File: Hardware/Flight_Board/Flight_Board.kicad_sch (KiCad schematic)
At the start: 5 parts, among them J1 Conn_01x04, J2 Conn_01x08

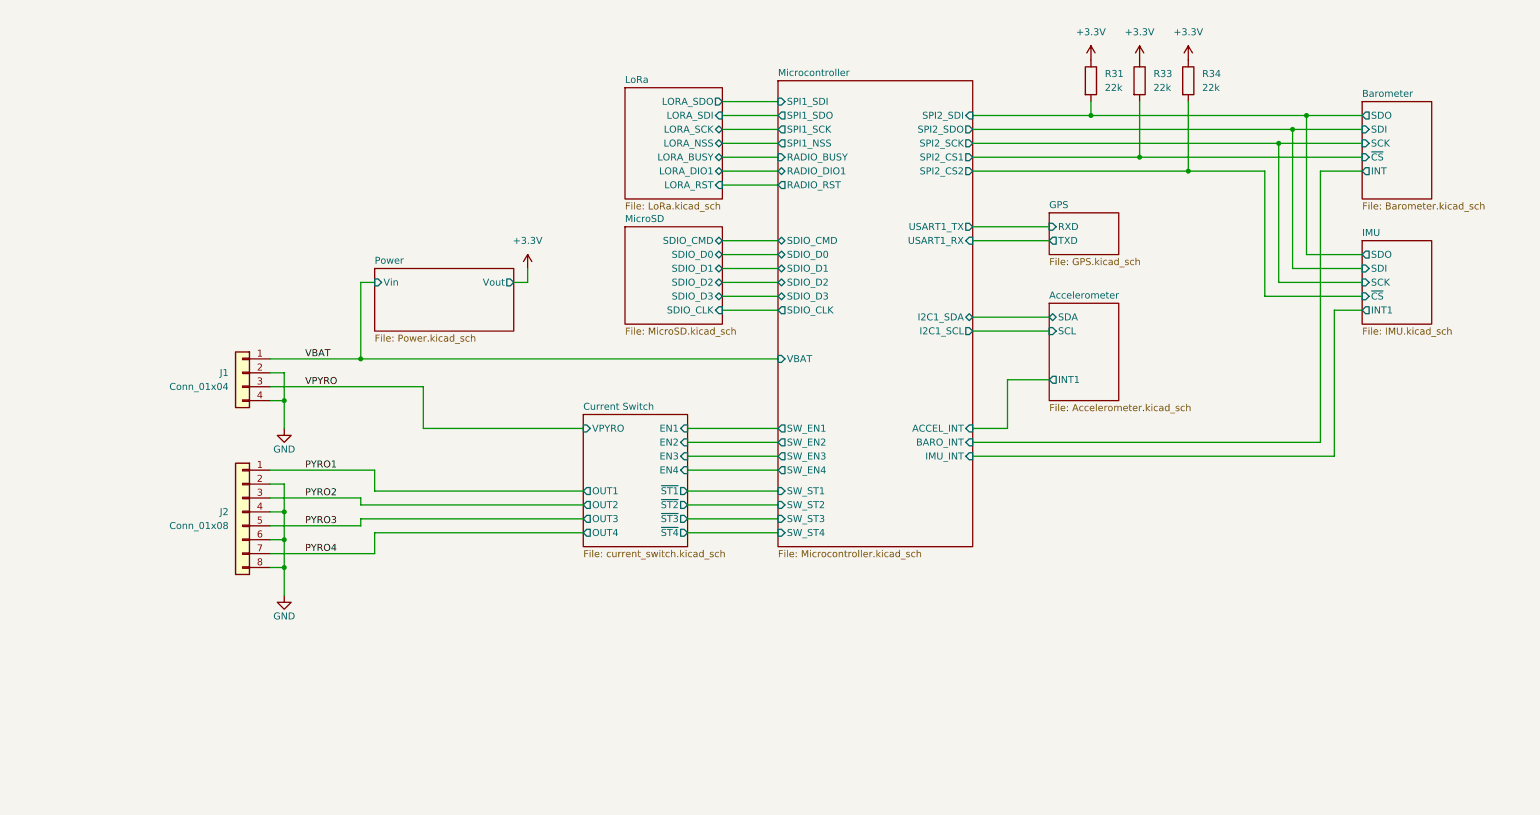
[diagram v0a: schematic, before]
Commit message: Add LEDs and test points
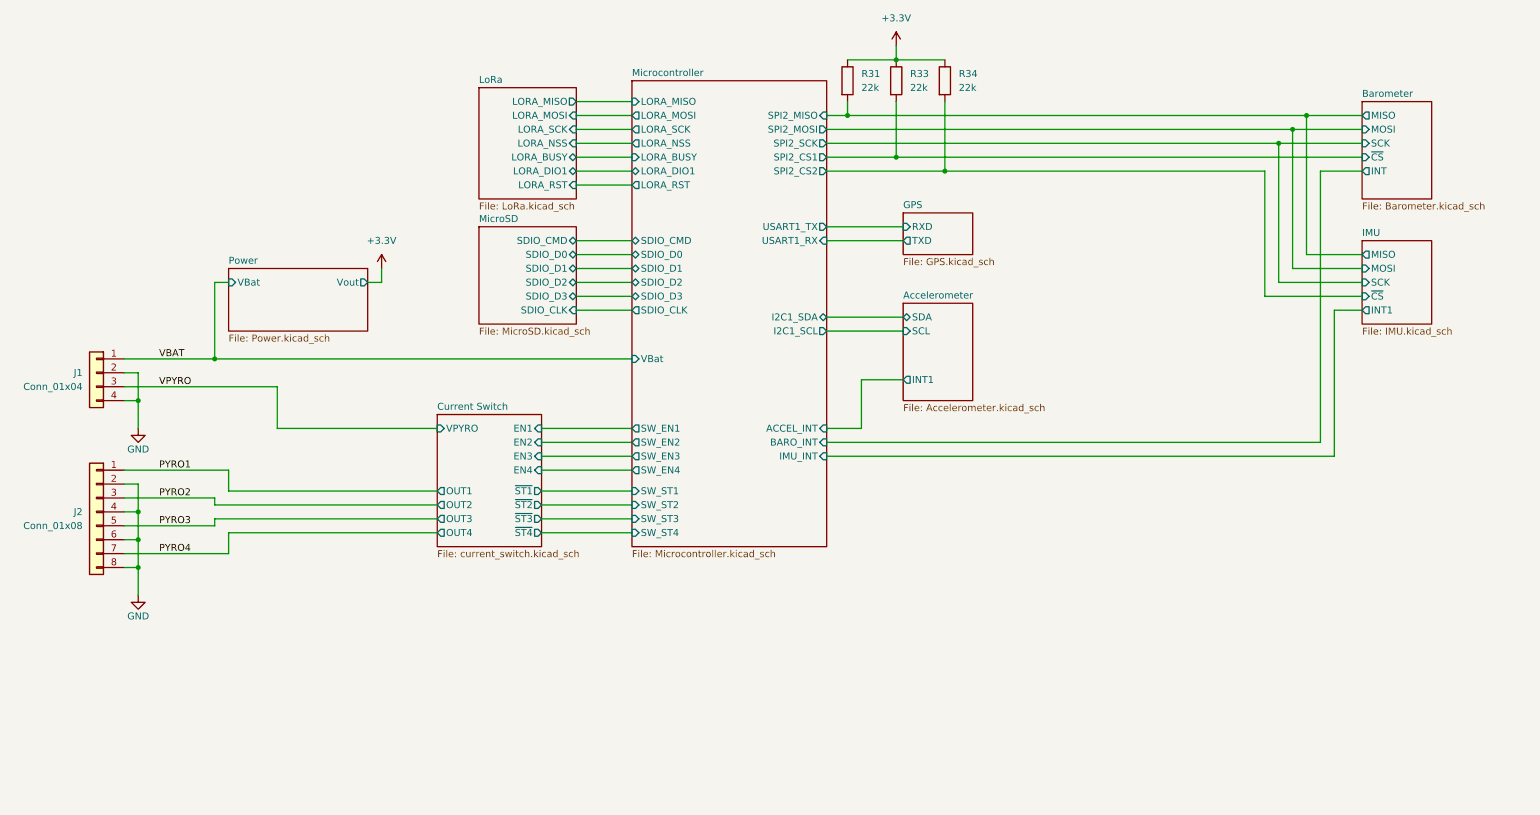
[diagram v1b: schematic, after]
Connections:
- net Barometer/SDO renamed Barometer/MISO
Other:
- sheet Barometer ports: added MISO, MOSI; removed SDI, SDO
- sheet IMU ports: added MISO, MOSI; removed SDI, SDO
- sheet LoRa ports: added LORA_MISO, LORA_MOSI; removed LORA_SDI, LORA_SDO
- sheet Microcontroller ports: added LORA_BUSY, LORA_DIO1, LORA_MISO, LORA_MOSI, LORA_NSS, LORA_RST, LORA_SCK, SPI2_MISO, SPI2_MOSI, VBat; removed RADIO_BUSY, RADIO_DIO1, RADIO_RST, SPI1_NSS, SPI1_SCK, SPI1_SDI, SPI1_SDO, SPI2_SDI, SPI2_SDO, VBAT
- sheet Power ports: added VBat; removed Vin
- moved on the sheet: J1, J2, R31, R33, R34

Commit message: final touches, bom, footprints
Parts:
- added TP1 (x4): GND, TestPoint:TestPoint_THTPad_2.0x2.0mm_Drill1.0mm, symbol Connector:TestPoint
- added TP1: VBAT, TestPoint:TestPoint_THTPad_2.0x2.0mm_Drill1.0mm, symbol Connector:TestPoint
- added TP1: VPYRO, TestPoint:TestPoint_THTPad_2.0x2.0mm_Drill1.0mm, symbol Connector:TestPoint
- J1: footprint (none) -> TerminalBlock_Phoenix:TerminalBlock_Phoenix_PT-1,5-4-3.5-H_1x04_P3.50mm_Horizontal
- J2: footprint (none) -> TerminalBlock_Phoenix:TerminalBlock_Phoenix_PT-1,5-8-3.5-H_1x08_P3.50mm_Horizontal
- R31, R33, R34: footprint (none) -> Resistor_SMD:R_0603_1608Metric_Pad0.98x0.95mm_HandSolder
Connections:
- net GND: now also TP1.1, TP1.1, TP1.1, TP1.1
- net VBAT: now also TP1.1
- net VPYRO: now also TP1.1

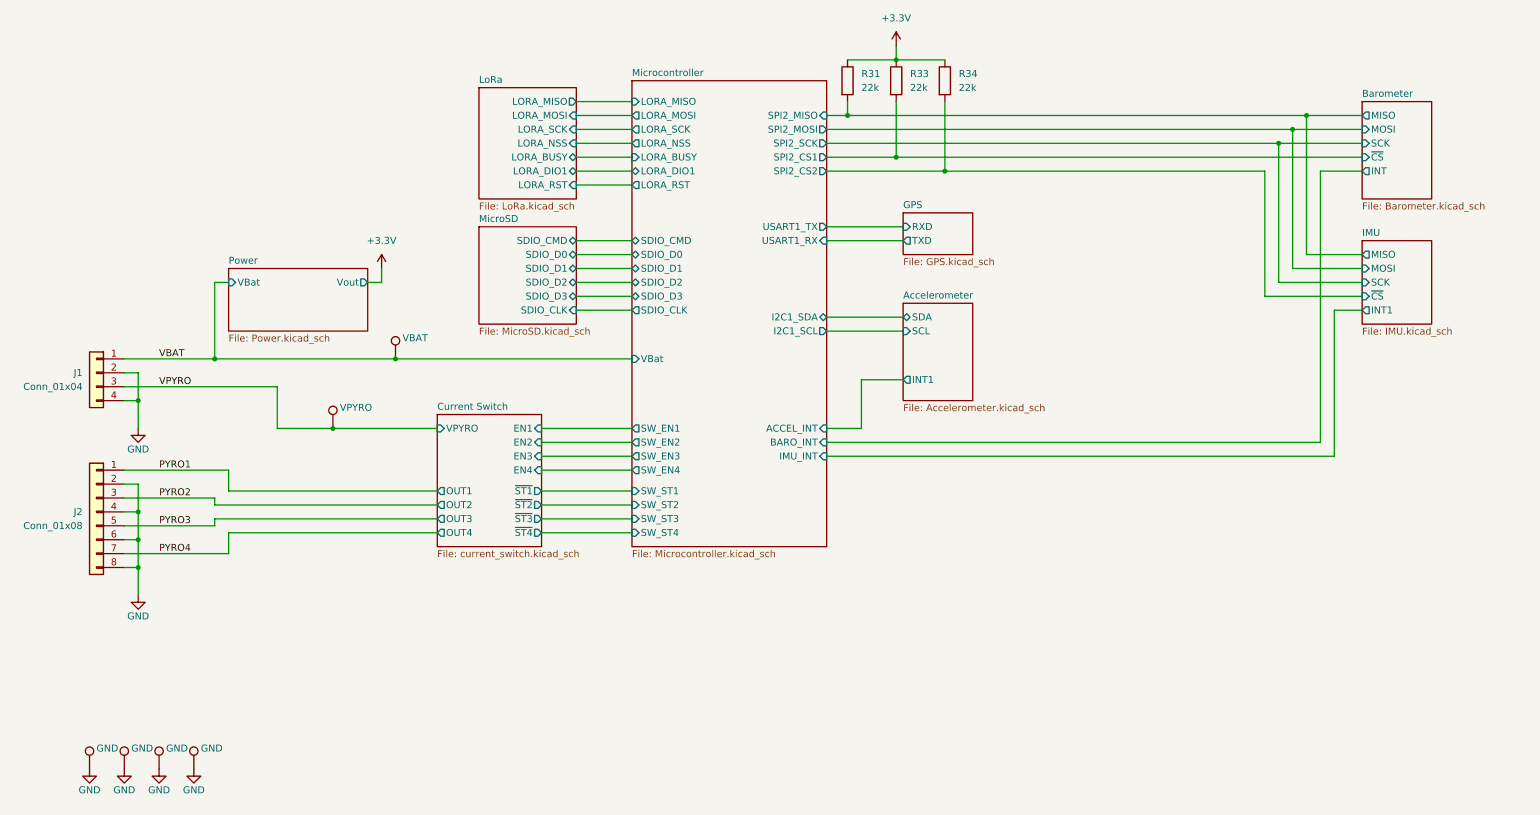
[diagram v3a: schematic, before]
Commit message: initial placement on board, continue routing
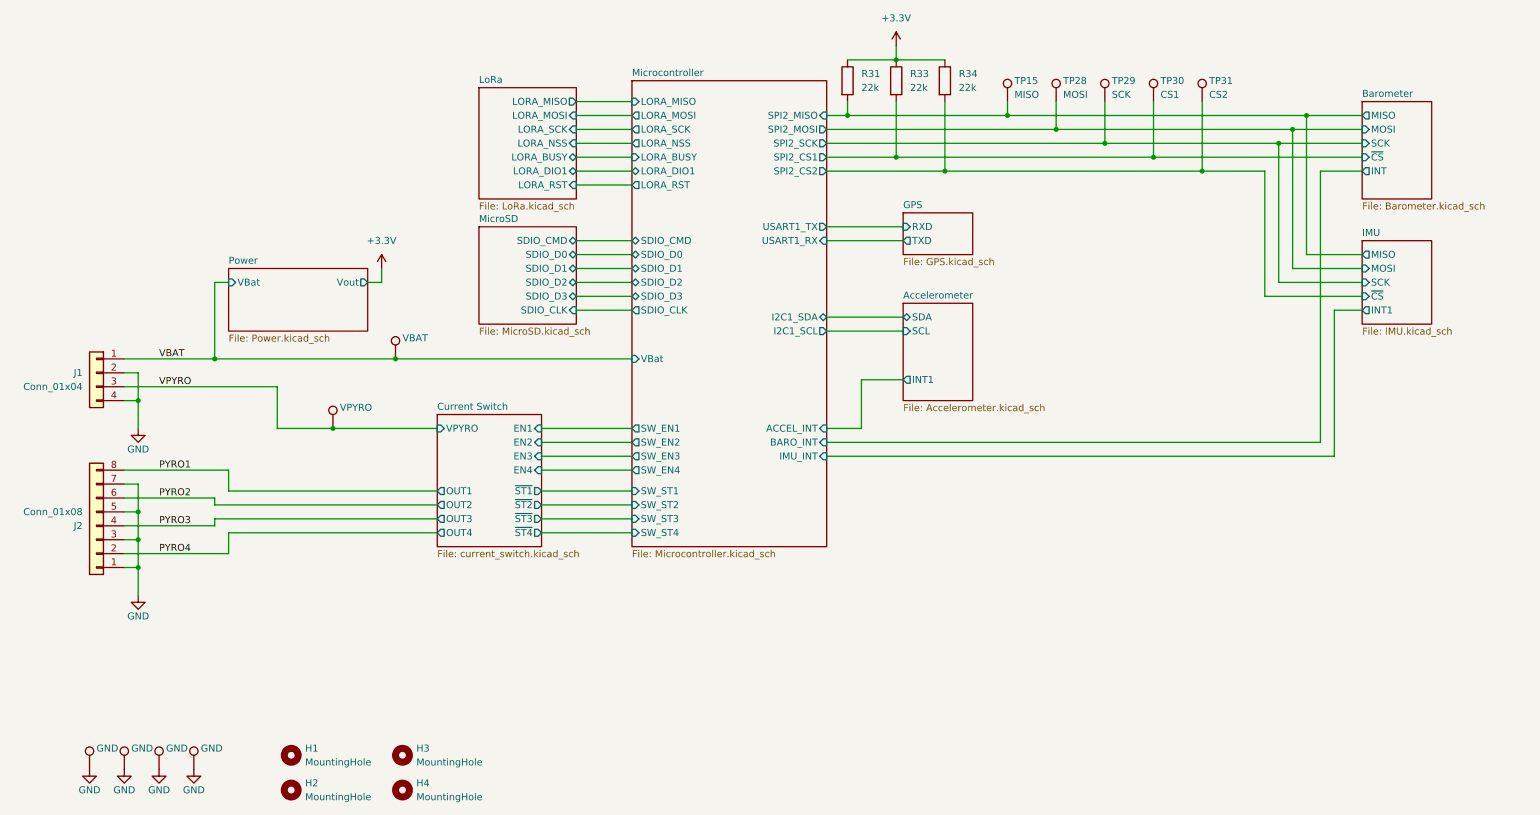
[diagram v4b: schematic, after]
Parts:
- added H1, H2, H3, H4: MountingHole, MountingHole:MountingHole_3.2mm_M3, symbol Mechanical:MountingHole
- added TP15: MISO, TestPoint:TestPoint_THTPad_2.0x2.0mm_Drill1.0mm, symbol Connector:TestPoint
- added TP28: MOSI, TestPoint:TestPoint_THTPad_2.0x2.0mm_Drill1.0mm, symbol Connector:TestPoint
- added TP29: SCK, TestPoint:TestPoint_THTPad_2.0x2.0mm_Drill1.0mm, symbol Connector:TestPoint
- added TP30: CS1, TestPoint:TestPoint_THTPad_2.0x2.0mm_Drill1.0mm, symbol Connector:TestPoint
- added TP31: CS2, TestPoint:TestPoint_THTPad_2.0x2.0mm_Drill1.0mm, symbol Connector:TestPoint
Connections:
- net Barometer/MISO: now also TP15.1
- net Barometer/MOSI: now also TP28.1
- net Barometer/SCK: now also TP29.1
- net Barometer/~{CS}: now also TP30.1
- net GND: now also J2.1 (Pin_1), J2.3 (Pin_3), J2.5 (Pin_5), J2.7 (Pin_7); no longer J2.2 (Pin_2), J2.4 (Pin_4), J2.6 (Pin_6), J2.8 (Pin_8)
- net IMU/~{CS}: now also TP31.1
- net PYRO1: now also J2.8 (Pin_8); no longer J2.1 (Pin_1)
- net PYRO2: now also J2.6 (Pin_6); no longer J2.3 (Pin_3)
- net PYRO3: now also J2.4 (Pin_4); no longer J2.5 (Pin_5)
- net PYRO4: now also J2.2 (Pin_2); no longer J2.7 (Pin_7)
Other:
- moved on the sheet: J2

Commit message: begin 4 layer board
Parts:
- H1, H2, H3, H4: footprint MountingHole:MountingHole_3.2mm_M3 -> MountingHole:MountingHole_3.2mm_M3_ISO14580
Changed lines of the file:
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@@
       (effects (font (size 1.27 1.27)) (justify left))
     )
-    (property "Footprint" "MountingHole:MountingHole_3.2mm_M3" (at 63.5 185.42 0)
+    (property "Footprint" "MountingHole:MountingHole_3.2mm_M3_ISO14580" (at 63.5 185.42 0)
       (effects (font (size 1.27 1.27)) hide)
     )
@@
       (effects (font (size 1.27 1.27)) (justify left))
     )
-    (property "Footprint" "MountingHole:MountingHole_3.2mm_M3" (at 83.82 185.42 0)
+    (property "Footprint" "MountingHole:MountingHole_3.2mm_M3_ISO14580" (at 83.82 185.42 0)
       (effects (font (size 1.27 1.27)) hide)
     )
@@
       (effects (font (size 1.27 1.27)) (justify left))
     )
-    (property "Footprint" "MountingHole:MountingHole_3.2mm_M3" (at 63.5 179.07 0)
+    (property "Footprint" "MountingHole:MountingHole_3.2mm_M3_ISO14580" (at 63.5 179.07 0)
       (effects (font (size 1.27 1.27)) hide)
     )
@@
       (effects (font (size 1.27 1.27)) (justify left))
     )
-    (property "Footprint" "MountingHole:MountingHole_3.2mm_M3" (at 83.82 179.07 0)
-      (effects (font (size 1.27 1.27)) hide)
-    )
+    (property "Footprint" "MountingHole:MountingHole_3.2mm_M3_ISO14580" (at 83.82 179.07 0)
+      (effects (font (size 1.27 1.27)) hide)
+    )

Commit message: initial route of 4-layer board
ouch
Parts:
- removed TP1: VBAT, TestPoint:TestPoint_THTPad_2.0x2.0mm_Drill1.0mm, symbol Connector:TestPoint
- removed TP1: VPYRO, TestPoint:TestPoint_THTPad_2.0x2.0mm_Drill1.0mm, symbol Connector:TestPoint
- renumbered R31 to R1, R33 to R2, R34 to R3, TP15 to TP5, TP28 to TP6, TP29 to TP7, TP30 to TP8, TP31 to TP9
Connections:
- net Barometer/~{CS} renamed CS1
- net IMU/~{CS} renamed CS2

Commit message: minor tweaks and prettification
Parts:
- TP1, TP5, TP6, TP7, TP8, TP9: footprint TestPoint:TestPoint_THTPad_2.0x2.0mm_Drill1.0mm -> TestPoint:TestPoint_Pad_D1.0mm
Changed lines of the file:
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@@
       (effects (font (size 1.27 1.27)) (justify left))
     )
-    (property "Footprint" "TestPoint:TestPoint_THTPad_2.0x2.0mm_Drill1.0mm" (at 50.8 181.61 0)
+    (property "Footprint" "TestPoint:TestPoint_Pad_D1.0mm" (at 50.8 181.61 0)
       (effects (font (size 1.27 1.27)) hide)
     )
@@
       (effects (font (size 1.27 1.27)) (justify left))
     )
-    (property "Footprint" "TestPoint:TestPoint_THTPad_2.0x2.0mm_Drill1.0mm" (at 234.95 59.69 0)
+    (property "Footprint" "TestPoint:TestPoint_Pad_D1.0mm" (at 234.95 59.69 0)
       (effects (font (size 1.27 1.27)) hide)
     )
@@
       (effects (font (size 1.27 1.27)) (justify left))
     )
-    (property "Footprint" "TestPoint:TestPoint_THTPad_2.0x2.0mm_Drill1.0mm" (at 38.1 181.61 0)
+    (property "Footprint" "TestPoint:TestPoint_Pad_D1.0mm" (at 38.1 181.61 0)
       (effects (font (size 1.27 1.27)) hide)
     )
@@
       (effects (font (size 1.27 1.27)) (justify left))
     )
-    (property "Footprint" "TestPoint:TestPoint_THTPad_2.0x2.0mm_Drill1.0mm" (at 31.75 181.61 0)
+    (property "Footprint" "TestPoint:TestPoint_Pad_D1.0mm" (at 31.75 181.61 0)
       (effects (font (size 1.27 1.27)) hide)
     )
@@
       (effects (font (size 1.27 1.27)) (justify left))
     )
-    (property "Footprint" "TestPoint:TestPoint_THTPad_2.0x2.0mm_Drill1.0mm" (at 44.45 181.61 0)
+    (property "Footprint" "TestPoint:TestPoint_Pad_D1.0mm" (at 44.45 181.61 0)
       (effects (font (size 1.27 1.27)) hide)
     )
@@
       (effects (font (size 1.27 1.27)) (justify left))
     )
-    (property "Footprint" "TestPoint:TestPoint_THTPad_2.0x2.0mm_Drill1.0mm" (at 199.39 59.69 0)
+    (property "Footprint" "TestPoint:TestPoint_Pad_D1.0mm" (at 199.39 59.69 0)
       (effects (font (size 1.27 1.27)) hide)
     )
@@
       (effects (font (size 1.27 1.27)) (justify left))
     )
-    (property "Footprint" "TestPoint:TestPoint_THTPad_2.0x2.0mm_Drill1.0mm" (at 208.28 59.69 0)
+    (property "Footprint" "TestPoint:TestPoint_Pad_D1.0mm" (at 208.28 59.69 0)
       (effects (font (size 1.27 1.27)) hide)
     )
@@
       (effects (font (size 1.27 1.27)) (justify left))
     )
-    (property "Footprint" "TestPoint:TestPoint_THTPad_2.0x2.0mm_Drill1.0mm" (at 226.06 59.69 0)
+    (property "Footprint" "TestPoint:TestPoint_Pad_D1.0mm" (at 226.06 59.69 0)
       (effects (font (size 1.27 1.27)) hide)
     )
@@
       (effects (font (size 1.27 1.27)) (justify left))
     )
-    (property "Footprint" "TestPoint:TestPoint_THTPad_2.0x2.0mm_Drill1.0mm" (at 217.17 59.69 0)
-      (effects (font (size 1.27 1.27)) hide)
-    )
+    (property "Footprint" "TestPoint:TestPoint_Pad_D1.0mm" (at 217.17 59.69 0)
+      (effects (font (size 1.27 1.27)) hide)
+    )

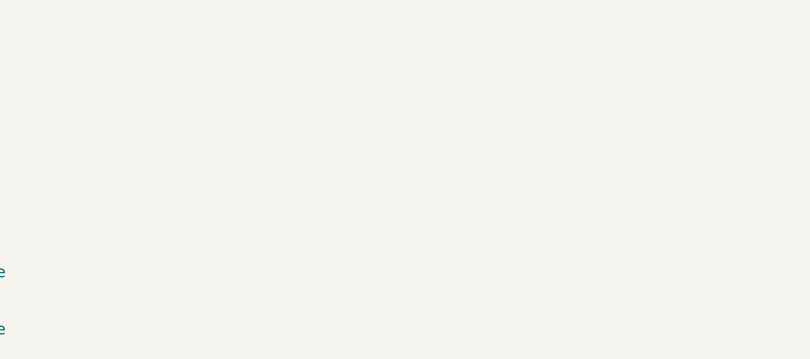
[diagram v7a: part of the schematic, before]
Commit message: add stencil holes
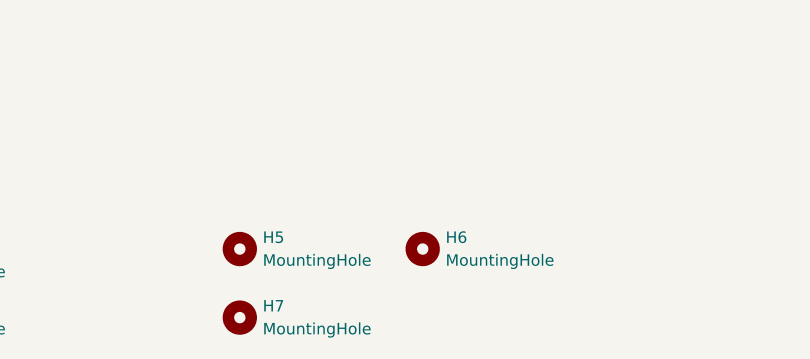
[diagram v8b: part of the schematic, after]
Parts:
- added H5, H6, H7: MountingHole, Project:Stencil_hole, symbol Mechanical:MountingHole
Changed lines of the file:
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@@
+    )
+  )
+  (symbol (lib_id "Mechanical:MountingHole") (at 124.46 177.8 0) (unit 1)
+    (in_bom yes) (on_board yes) (dnp no) (fields_autoplaced)
+    (property "Reference" "H5" (at 127 176.53 0)
+      (effects (font (size 1.27 1.27)) (justify left))
+    )
+    (property "Value" "MountingHole" (at 127 179.07 0)
+      (effects (font (size 1.27 1.27)) (justify left))
+    )
+    (property "Footprint" "Project:Stencil_hole" (at 124.46 177.8 0)
+      (effects (font (size 1.27 1.27)) hide)
+    )
+    (property "Datasheet" "~" (at 124.46 177.8 0)
+      (effects (font (size 1.27 1.27)) hide)
+    )
+    (instances
+      (project "Flight_Board"
+        (path "/e8eb85d5-f1ff-4500-895d-25b9ff5f6d36"
+          (reference "H5") (unit 1)
+        )
+      )
     )
   )
@@
     )
   )
+  (symbol (lib_id "Mechanical:MountingHole") (at 124.46 185.42 0) (unit 1)
+    (in_bom yes) (on_board yes) (dnp no) (fields_autoplaced)
+    (property "Reference" "H7" (at 127 184.15 0)
+      (effects (font (size 1.27 1.27)) (justify left))
+    )
+    (property "Value" "MountingHole" (at 127 186.69 0)
+      (effects (font (size 1.27 1.27)) (justify left))
+    )
+    (property "Footprint" "Project:Stencil_hole" (at 124.46 185.42 0)
+      (effects (font (size 1.27 1.27)) hide)
+    )
+    (property "Datasheet" "~" (at 124.46 185.42 0)
+      (effects (font (size 1.27 1.27)) hide)
+    )
+    (instances
+      (project "Flight_Board"
+        (path "/e8eb85d5-f1ff-4500-895d-25b9ff5f6d36"
+          (reference "H7") (unit 1)
+        )
+      )
+    )
+  )
   (symbol (lib_id "Connector:TestPoint") (at 26.67 181.61 0) (unit 1)
     (in_bom yes) (on_board yes) (dnp no)
@@
         )
       )
+    )
+  )
+  (symbol (lib_id "Mechanical:MountingHole") (at 144.78 177.8 0) (unit 1)
+    (in_bom yes) (on_board yes) (dnp no) (fields_autoplaced)
+    (property "Reference" "H6" (at 147.32 176.53 0)
+      (effects (font (size 1.27 1.27)) (justify left))
+    )
+    (property "Value" "MountingHole" (at 147.32 179.07 0)
+      (effects (font (size 1.27 1.27)) (justify left))
+    )
+    (property "Footprint" "Project:Stencil_hole" (at 144.78 177.8 0)
+      (effects (font (size 1.27 1.27)) hide)
+    )
+    (property "Datasheet" "~" (at 144.78 177.8 0)
+      (effects (font (size 1.27 1.27)) hide)
+    )
+    (instances
+      (project "Flight_Board"
+        (path "/e8eb85d5-f1ff-4500-895d-25b9ff5f6d36"
+          (reference "H6") (unit 1)
+        )
+      )
